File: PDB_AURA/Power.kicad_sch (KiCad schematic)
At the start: 36 parts, among them J100 XT30PW-M, U101 SI4825DDY-T1-GE3, U2 TPS56C230RJER

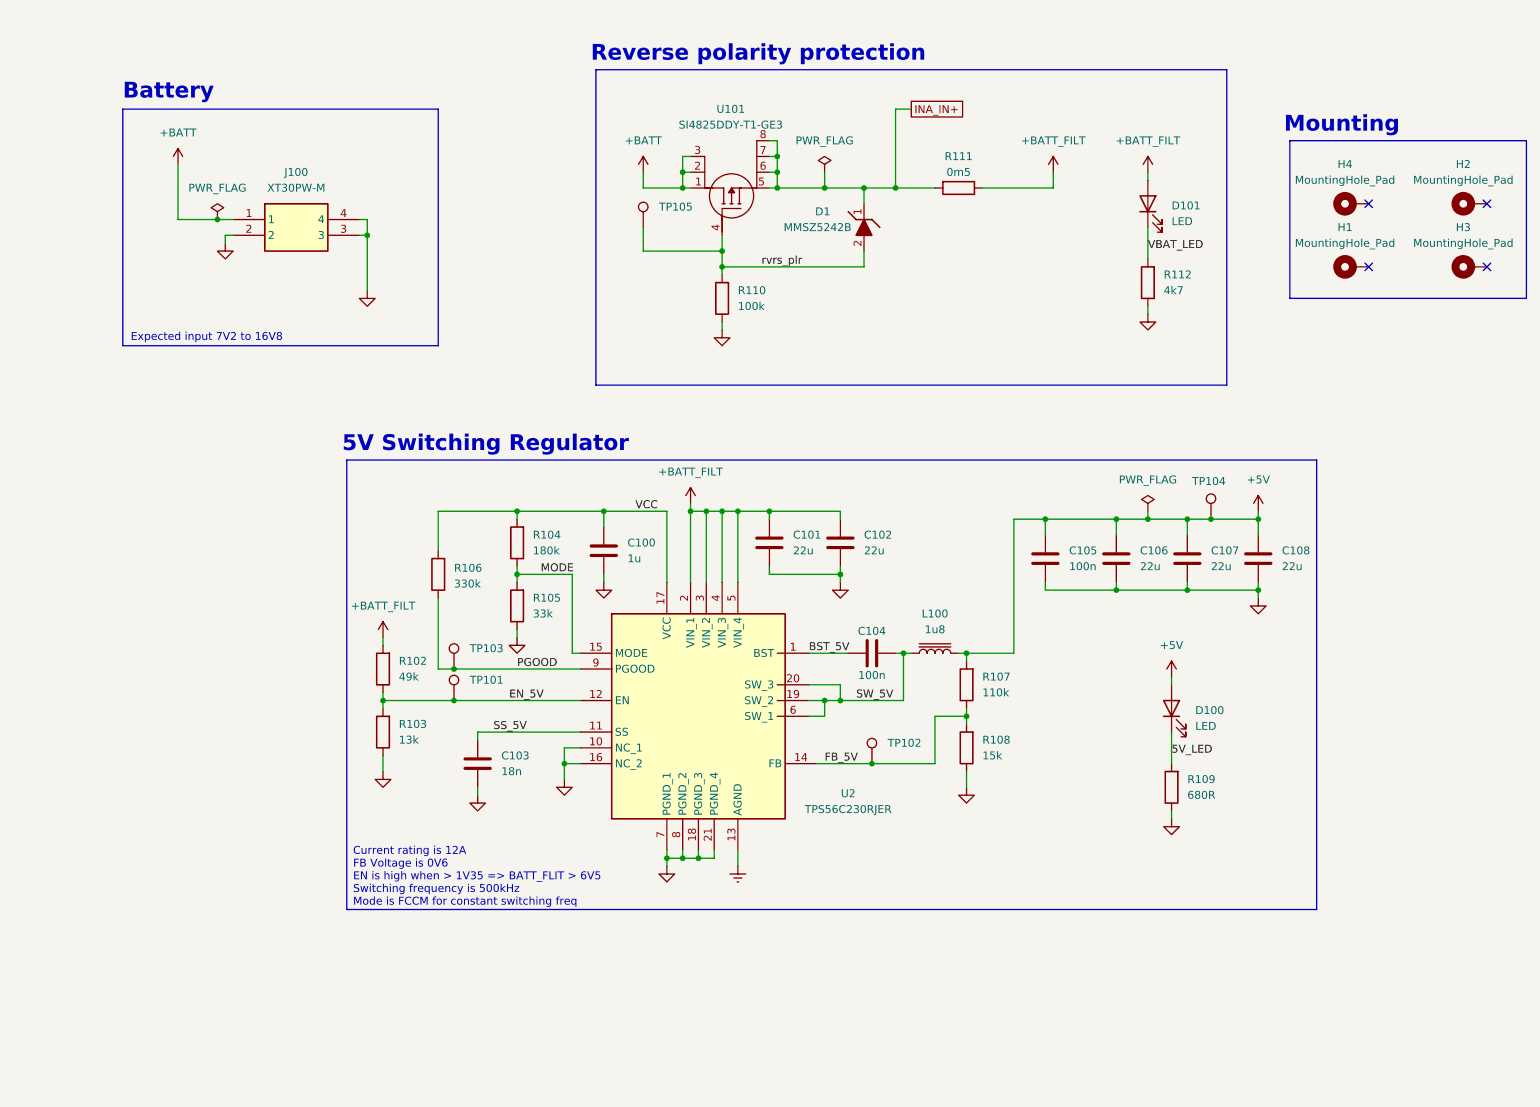
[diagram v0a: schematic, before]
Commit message: New PDB specs chosen
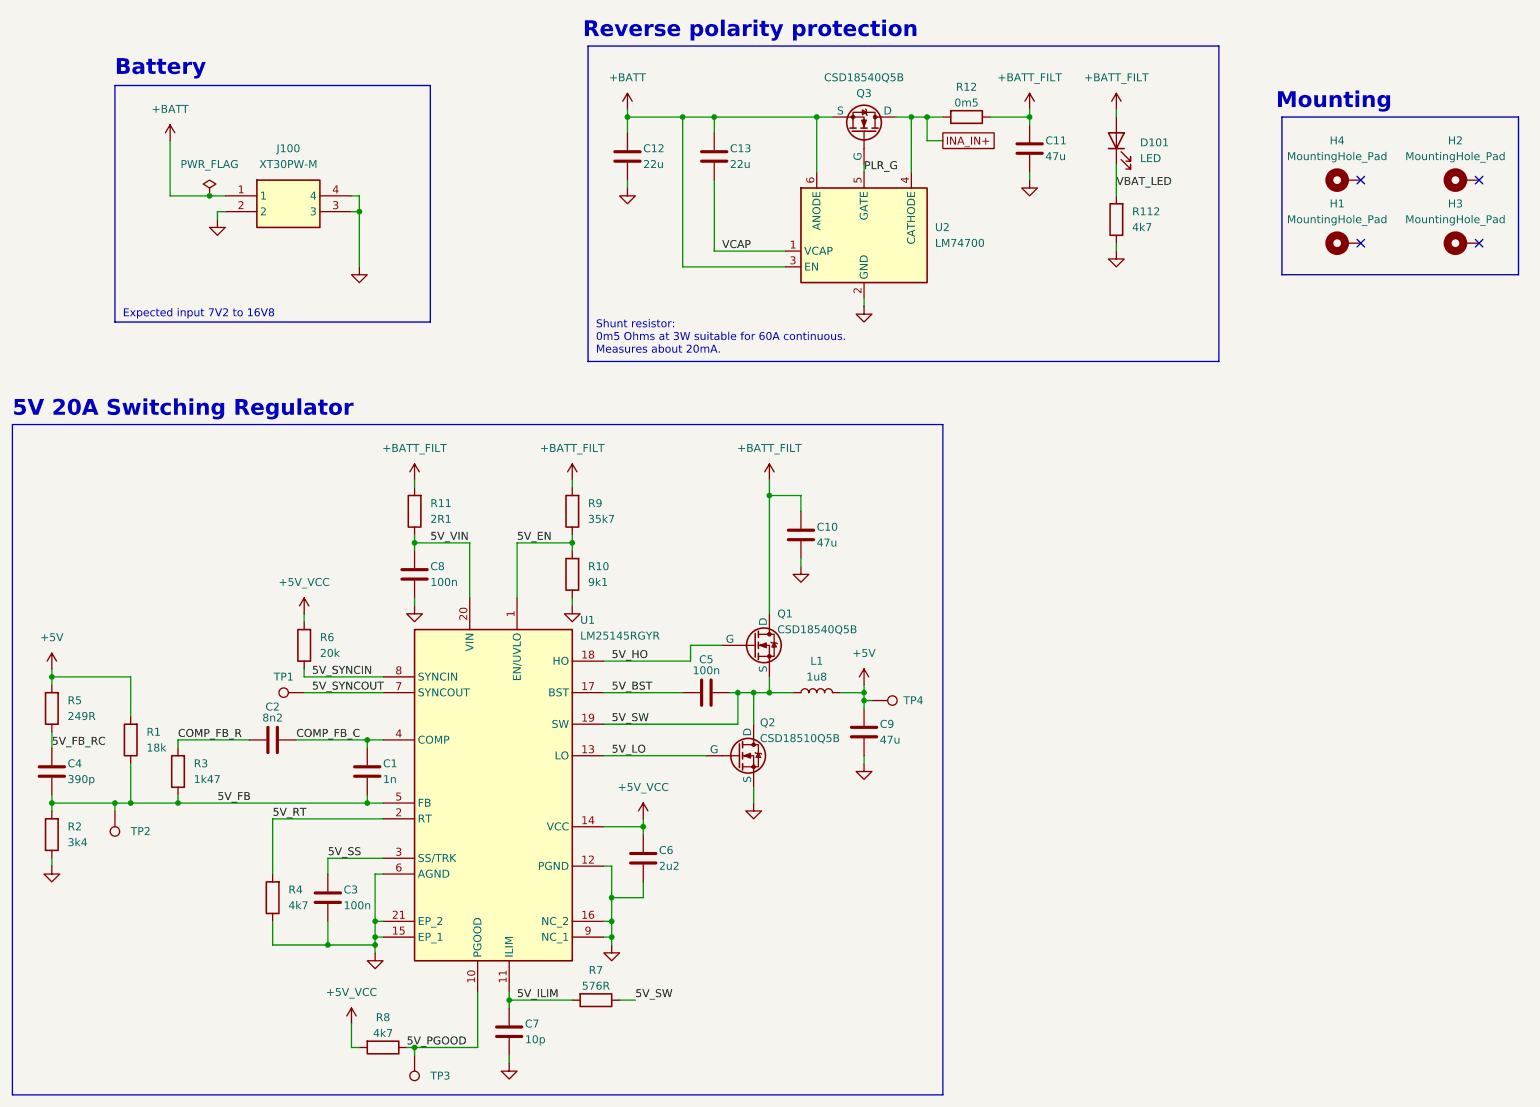
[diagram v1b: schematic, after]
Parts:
- removed C100: 1u, Capacitor_SMD:C_0402_1005Metric, symbol Device:C
- removed C101, C102: 22u, Capacitor_SMD:C_1206_3216Metric, symbol Device:C
- removed C103: 18n, Capacitor_SMD:C_0402_1005Metric, symbol Device:C
- removed C104: 100n, Capacitor_SMD:C_0402_1005Metric, symbol Device:C
- removed C105: 100n, Capacitor_SMD:C_0603_1608Metric, symbol Device:C
- removed C106, C107, C108: 22u, Capacitor_SMD:C_0805_2012Metric, symbol Device:C
- removed D1: MMSZ5242B, MMSZ5252B:MMSZ5252B, symbol MMSZ5252B:MMSZ5242B
- removed D100: LED, LED_SMD:LED_0603_1608Metric, symbol Device:LED
- removed L100: 1u8, CKST0603:CKST0603-1.5uHM, symbol Device:L_Iron
- removed R102: 49k, Resistor_SMD:R_0402_1005Metric, symbol Device:R
- removed R103: 13k, Resistor_SMD:R_0402_1005Metric, symbol Device:R
- removed R104: 180k, Resistor_SMD:R_0402_1005Metric, symbol Device:R
- removed R105: 33k, Resistor_SMD:R_0402_1005Metric, symbol Device:R
- removed R106: 330k, Resistor_SMD:R_0402_1005Metric, symbol Device:R
- removed R107: 110k, Resistor_SMD:R_0402_1005Metric, symbol Device:R
- removed R108: 15k, Resistor_SMD:R_0402_1005Metric, symbol Device:R
- removed R109: 680R, Resistor_SMD:R_0402_1005Metric, symbol Device:R
- removed R110: 100k, Resistor_SMD:R_0402_1005Metric, symbol Device:R
- removed R111: 0m5, Resistor_SMD:R_1812_4532Metric, symbol Device:R
- removed TP101, TP102, TP103, TP104, TP105: TestPoint, TestPoint:TestPoint_Pad_D1.0mm, symbol Connector:TestPoint
- removed U101: SI4825DDY-T1-GE3, SI4825DDY-T1-GE3:SI4825DDY-T1-GE3, symbol SI4825DDY-T1-GE3:SI4825DDY-T1-GE3
- removed U2: TPS56C230RJER, TPS56C230RJER:QFN45P300X300X100-21N-D, symbol TPS56C230RJER:TPS56C230RJER
- added C1: 1n, Capacitor_SMD:C_0402_1005Metric, symbol Device:C
- added C10, C11, C9: 47u, Capacitor_SMD:C_1210_3225Metric, symbol Device:C
- added C12, C13: 22u, Capacitor_SMD:C_1210_3225Metric, symbol Device:C
- added C2: 8n2, Capacitor_SMD:C_0402_1005Metric, symbol Device:C
- added C3, C8: 100n, Capacitor_SMD:C_0402_1005Metric, symbol Device:C
- added C4: 390p, Capacitor_SMD:C_0402_1005Metric, symbol Device:C
- added C5: 100n, Resistor_SMD:R_0402_1005Metric, symbol Device:C
- added C6: 2u2, Capacitor_SMD:C_0402_1005Metric, symbol Device:C
- added C7: 10p, Capacitor_SMD:C_0402_1005Metric, symbol Device:C
- added L1: 1u8, 125CDMCCDS-1R8MC:Untitled, symbol Device:L
- added Q1, Q3: CSD18540Q5B, CSD18540Q5B:CSD18540Q5B, symbol Simulation_SPICE:NMOS
- added Q2: CSD18510Q5B, CSD18510Q5B:CSD18540Q5BT, symbol Simulation_SPICE:NMOS
- added R1: 18k, Resistor_SMD:R_0402_1005Metric, symbol Device:R
- added R10: 9k1, Resistor_SMD:R_0402_1005Metric, symbol Device:R
- added R11: 2R1, Resistor_SMD:R_0402_1005Metric, symbol Device:R
- added R12: 0m5, Resistor_SMD:R_2512_6332Metric, symbol Device:R
- added R2: 3k4, Resistor_SMD:R_0402_1005Metric, symbol Device:R
- added R3: 1k47, Resistor_SMD:R_0402_1005Metric, symbol Device:R
- added R4, R8: 4k7, Resistor_SMD:R_0402_1005Metric, symbol Device:R
- added R5: 249R, Resistor_SMD:R_0402_1005Metric, symbol Device:R
- added R6: 20k, Resistor_SMD:R_0402_1005Metric, symbol Device:R
- added R7: 576R, Resistor_SMD:R_0402_1005Metric, symbol Device:R
- added R9: 35k7, Resistor_SMD:R_0402_1005Metric, symbol Device:R
- added TP1, TP2, TP3, TP4: TestPoint, TestPoint:TestPoint_Pad_D1.0mm, symbol Connector:TestPoint
- added U1: LM25145RGYR, LM24145RGYR:RGY0020B, symbol LM25145RGYR:LM25145RGYR
- added U2: LM74700, Package_TO_SOT_SMD:SOT-23-6, symbol Power_Management:LM74700
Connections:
- net +5V: now also C9.1, L1.2, R1.2, R5.2, TP4.1
- net +BATT: now also C12.1, C13.1, Q3.3 (S), U2.3 (EN), U2.6 (ANODE)
- net +BATT_FILT: now also C10.1, C11.1, Q1.2 (D), R11.2, R12.1, R9.2
- net GND: now also C10.2, C11.2, C12.2, C3.2, C6.2, C7.2, C8.2, C9.2, Q2.3 (S), R10.1, R2.1, R4.1, U1.12 (PGND), U1.15 (EP_1), U1.16 (NC_2), U1.21 (EP_2), U1.6 (AGND), U1.9 (NC_1), U2.2 (GND)
- net INA_IN+: now also Q3.2 (D), R12.2, U2.4 (CATHODE)
- new net +5V_VCC: C6.1, R6.2, R8.2, U1.14 (VCC)
- new net 5V_BST: C5.1, U1.17 (BST)
- new net 5V_EN: R10.2, R9.1, U1.1 (EN/UVLO)
- new net 5V_FB: C1.2, C4.2, R1.1, R2.2, R3.1, TP2.1, U1.5 (FB)
- new net 5V_FB_RC: C4.1, R5.1
- new net 5V_HO: Q1.1 (G), U1.18 (HO)
- new net 5V_ILIM: C7.1, R7.2, U1.11 (ILIM)
- new net 5V_LO: Q2.1 (G), U1.13 (LO)
- new net 5V_PGOOD: R8.1, TP3.1, U1.10 (PGOOD)
- new net 5V_RT: R4.2, U1.2 (RT)
- new net 5V_SS: C3.1, U1.3 (SS/TRK)
- new net 5V_SW: C5.2, L1.1, Q1.3 (S), Q2.2 (D), R7.1, U1.19 (SW)
- new net 5V_SYNCIN: R6.1, U1.8 (SYNCIN)
- new net 5V_SYNCOUT: TP1.1, U1.7 (SYNCOUT)
- new net 5V_VIN: C8.1, R11.1, U1.20 (VIN)
- new net COMP_FB_C: C1.1, C2.2, U1.4 (COMP)
- new net COMP_FB_R: C2.1, R3.2
- new net PLR_G: Q3.1 (G), U2.5 (GATE)
- new net VCAP: C13.2, U2.1 (VCAP)
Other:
- note added: "5V 20A Switching Regulator"
- note added: "Shunt resistor: 0m5 Ohms at 3W suitable for 60A continuous. Measures about 20mA."
- note removed: "5V Switching Regulator"
- note removed: "Current rating is 12A FB Voltage is 0V6 EN is high when > 1V35 => BATT_FLIT > 6V5 Switching frequency is 500kHz Mode is FCCM for constant switching freq"
- moved on the sheet: D101, H1, H2, H3, H4, J100, R112

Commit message: Moving to laptop
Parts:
- removed C1: 1n, Capacitor_SMD:C_0402_1005Metric, symbol Device:C
- removed C10, C9: 47u, Capacitor_SMD:C_1210_3225Metric, symbol Device:C
- removed C2: 8n2, Capacitor_SMD:C_0402_1005Metric, symbol Device:C
- removed C3, C8: 100n, Capacitor_SMD:C_0402_1005Metric, symbol Device:C
- removed C4: 390p, Capacitor_SMD:C_0402_1005Metric, symbol Device:C
- removed C5: 100n, Resistor_SMD:R_0402_1005Metric, symbol Device:C
- removed C6: 2u2, Capacitor_SMD:C_0402_1005Metric, symbol Device:C
- removed C7: 10p, Capacitor_SMD:C_0402_1005Metric, symbol Device:C
- removed L1: 1u8, 125CDMCCDS-1R8MC:Untitled, symbol Device:L
- removed Q1: CSD18540Q5B, CSD18540Q5B:CSD18540Q5B, symbol Simulation_SPICE:NMOS
- removed Q2: CSD18510Q5B, CSD18510Q5B:CSD18540Q5BT, symbol Simulation_SPICE:NMOS
- removed R1: 18k, Resistor_SMD:R_0402_1005Metric, symbol Device:R
- removed R10: 9k1, Resistor_SMD:R_0402_1005Metric, symbol Device:R
- removed R11: 2R1, Resistor_SMD:R_0402_1005Metric, symbol Device:R
- removed R2: 3k4, Resistor_SMD:R_0402_1005Metric, symbol Device:R
- removed R3: 1k47, Resistor_SMD:R_0402_1005Metric, symbol Device:R
- removed R4, R8: 4k7, Resistor_SMD:R_0402_1005Metric, symbol Device:R
- removed R5: 249R, Resistor_SMD:R_0402_1005Metric, symbol Device:R
- removed R6: 20k, Resistor_SMD:R_0402_1005Metric, symbol Device:R
- removed R7: 576R, Resistor_SMD:R_0402_1005Metric, symbol Device:R
- removed R9: 35k7, Resistor_SMD:R_0402_1005Metric, symbol Device:R
- removed TP1, TP2, TP3, TP4: TestPoint, TestPoint:TestPoint_Pad_D1.0mm, symbol Connector:TestPoint
- removed U1: LM25145RGYR, LM24145RGYR:RGY0020B, symbol LM25145RGYR:LM25145RGYR
- added C16: 22u, Capacitor_SMD:C_1210_3225Metric, symbol Device:C
- added J10, J9: ~, SOLDER_PAD:BAT_SOLDER_PAD, symbol SOLDER_PAD:Power_Solder_Pad
- C11: value 47u -> 22u
- C13: value 22u -> 47n; footprint Capacitor_SMD:C_1210_3225Metric -> Capacitor_SMD:C_0402_1005Metric
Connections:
- net +BATT: now also J9.1
- net +BATT_FILT: no longer C11.1
- net GND: now also C16.2, J10.1
- net INA_IN+: now also C11.1, C16.1
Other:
- note removed: "5V 20A Switching Regulator"
- moved on the sheet: C11, D101, R112, R12

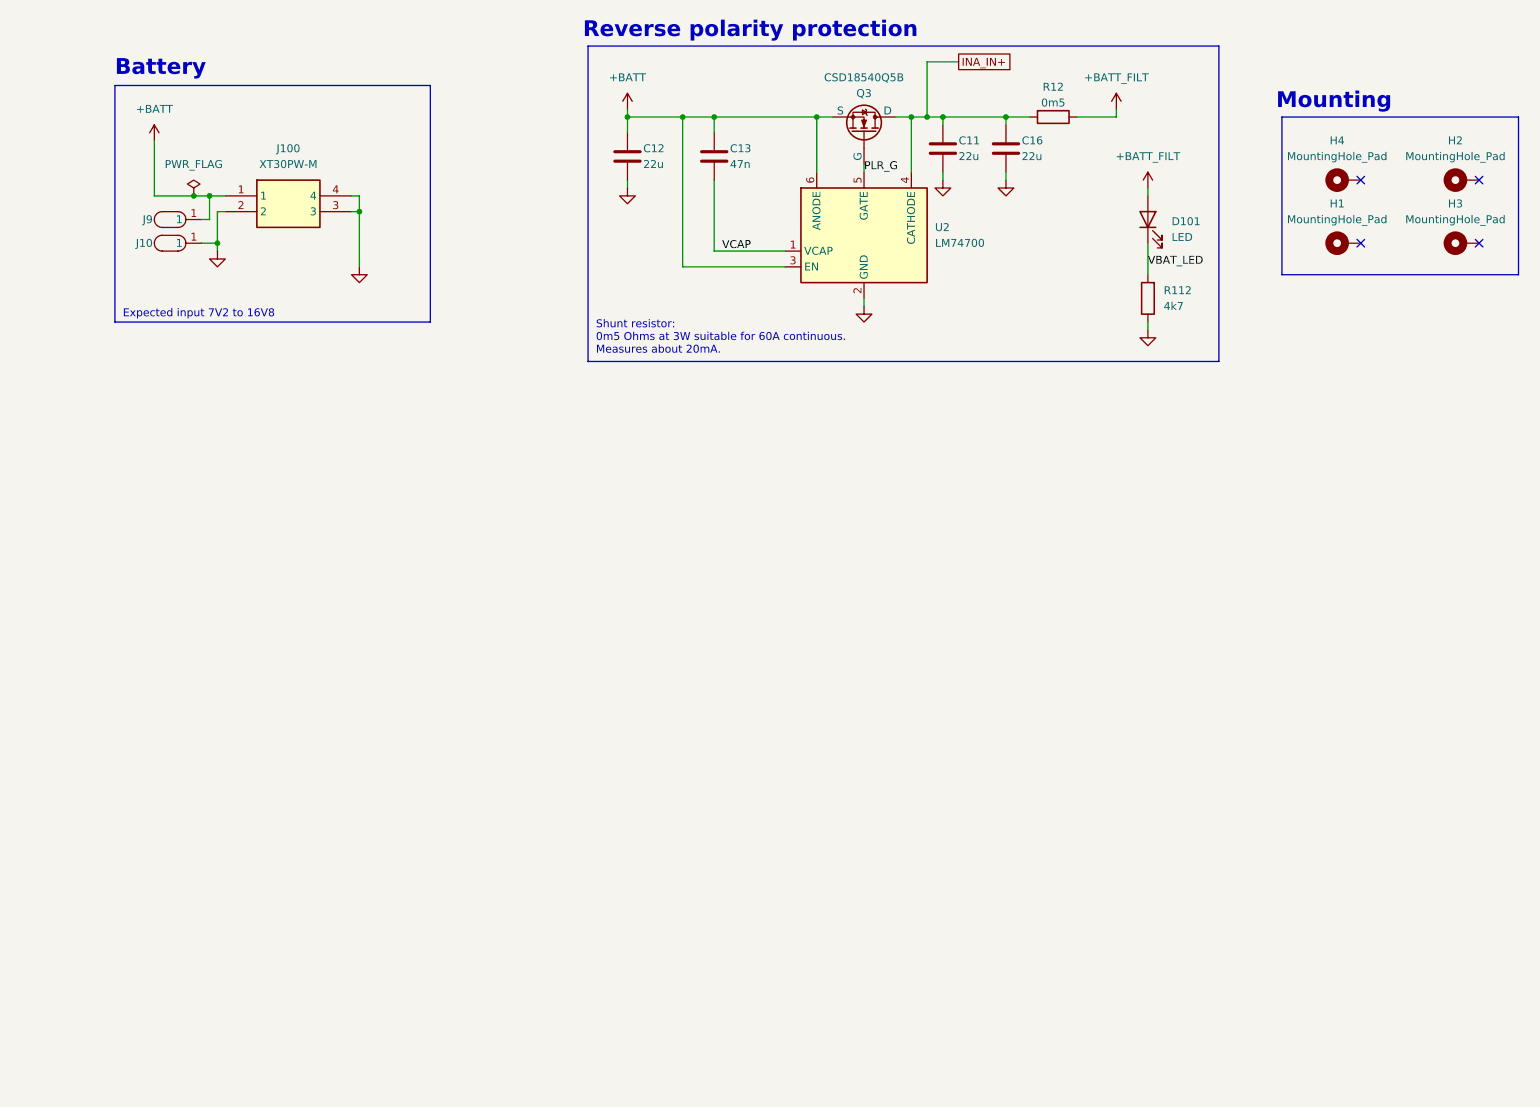
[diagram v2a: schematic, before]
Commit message: Annotated schematic for PDB
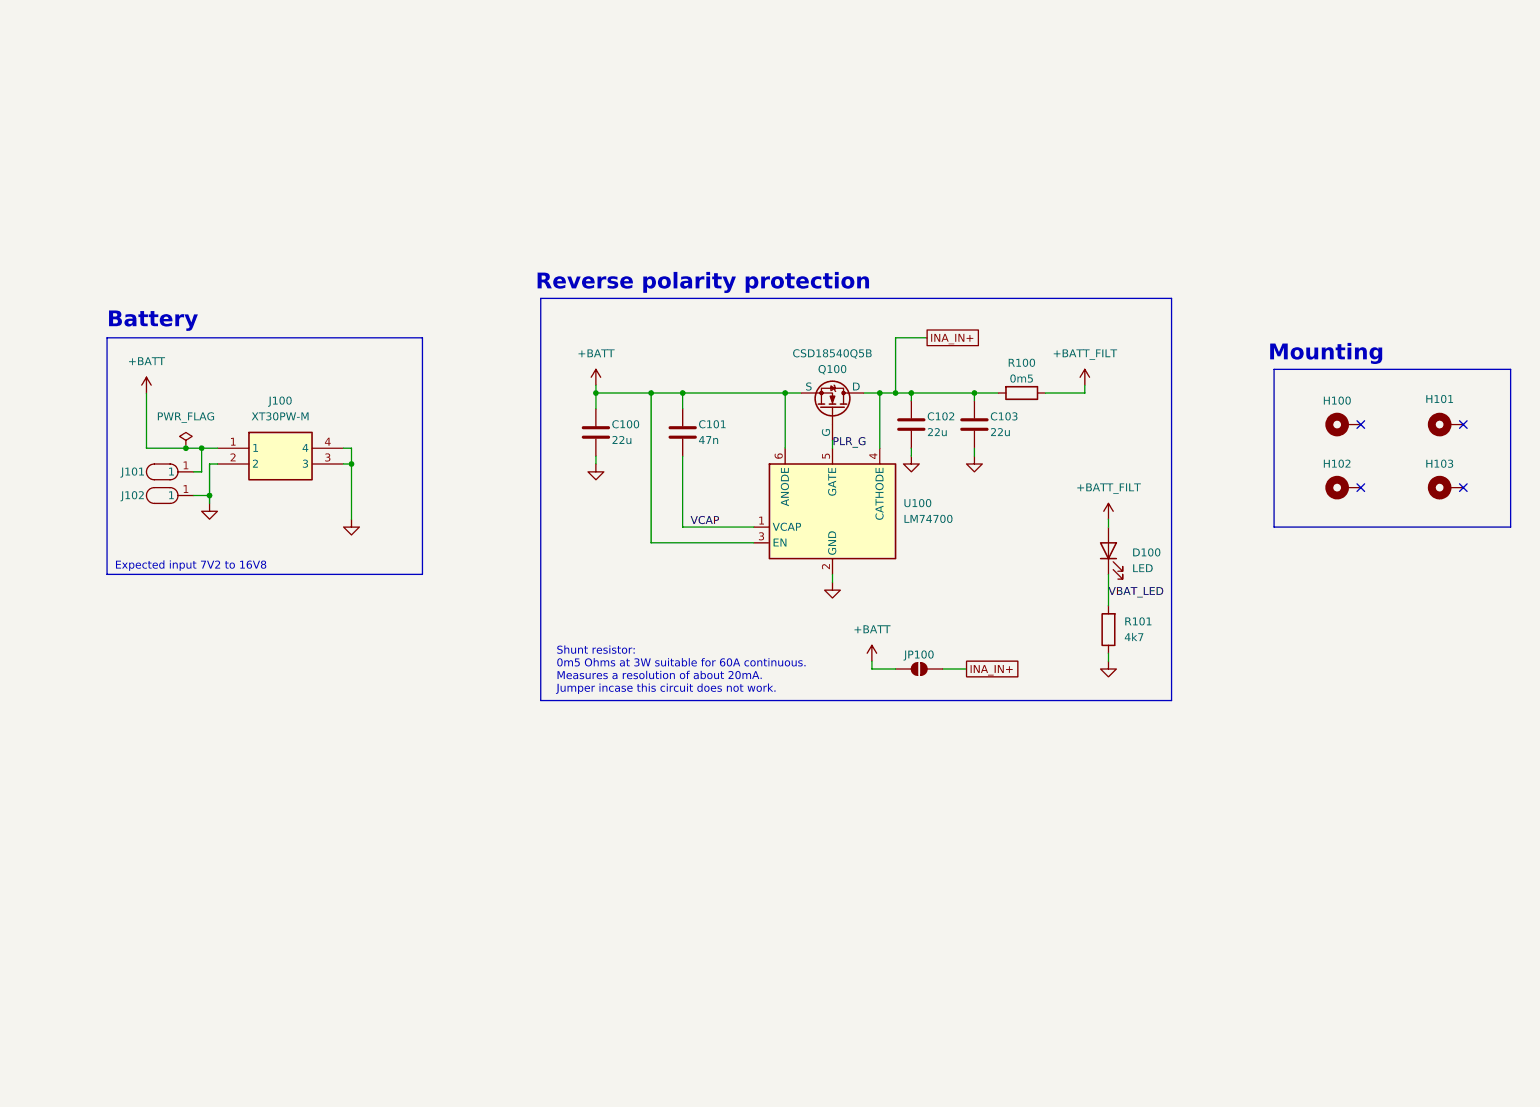
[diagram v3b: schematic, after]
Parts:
- added JP100: SolderJumper_2_Open, Jumper:SolderJumper-2_P1.3mm_Open_RoundedPad1.0x1.5mm, symbol Jumper:SolderJumper_2_Open
- renumbered C12 to C100, C13 to C101, C11 to C102, C16 to C103, D101 to D100, H4 to H100, H2 to H101, H1 to H102, H3 to H103, J9 to J101, J10 to J102, Q3 to Q100, R12 to R100, R112 to R101, U2 to U100
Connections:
- net +BATT: now also JP100.1 (A)
- net INA_IN+: now also JP100.2 (B)
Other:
- note added: "Shunt resistor: 0m5 Ohms at 3W suitable for 60A continuous. Measures a resolution of about 20mA. Jumper incase this circuit does not work."
- note removed: "Shunt resistor: 0m5 Ohms at 3W suitable for 60A continuous. Measures about 20mA."
- moved on the sheet: C100, C101, C102, C103, D100, H100, H101, H102, H103, J100, J101, J102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
